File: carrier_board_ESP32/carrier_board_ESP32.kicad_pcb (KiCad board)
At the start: 2 copper layers, 93.5 x 71 mm, 0 parts

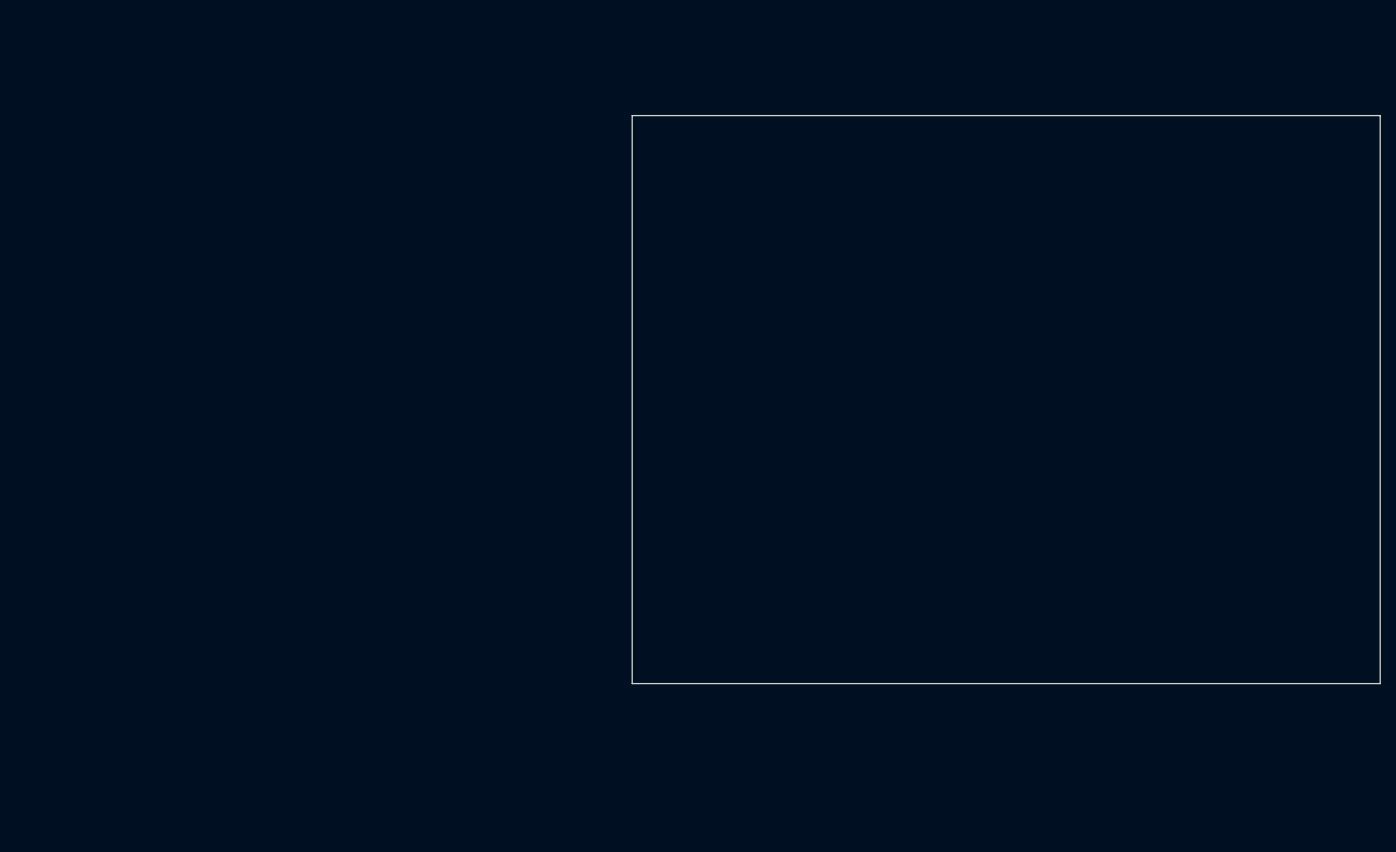
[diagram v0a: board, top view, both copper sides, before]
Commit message: added power supply (battery and solar panel)
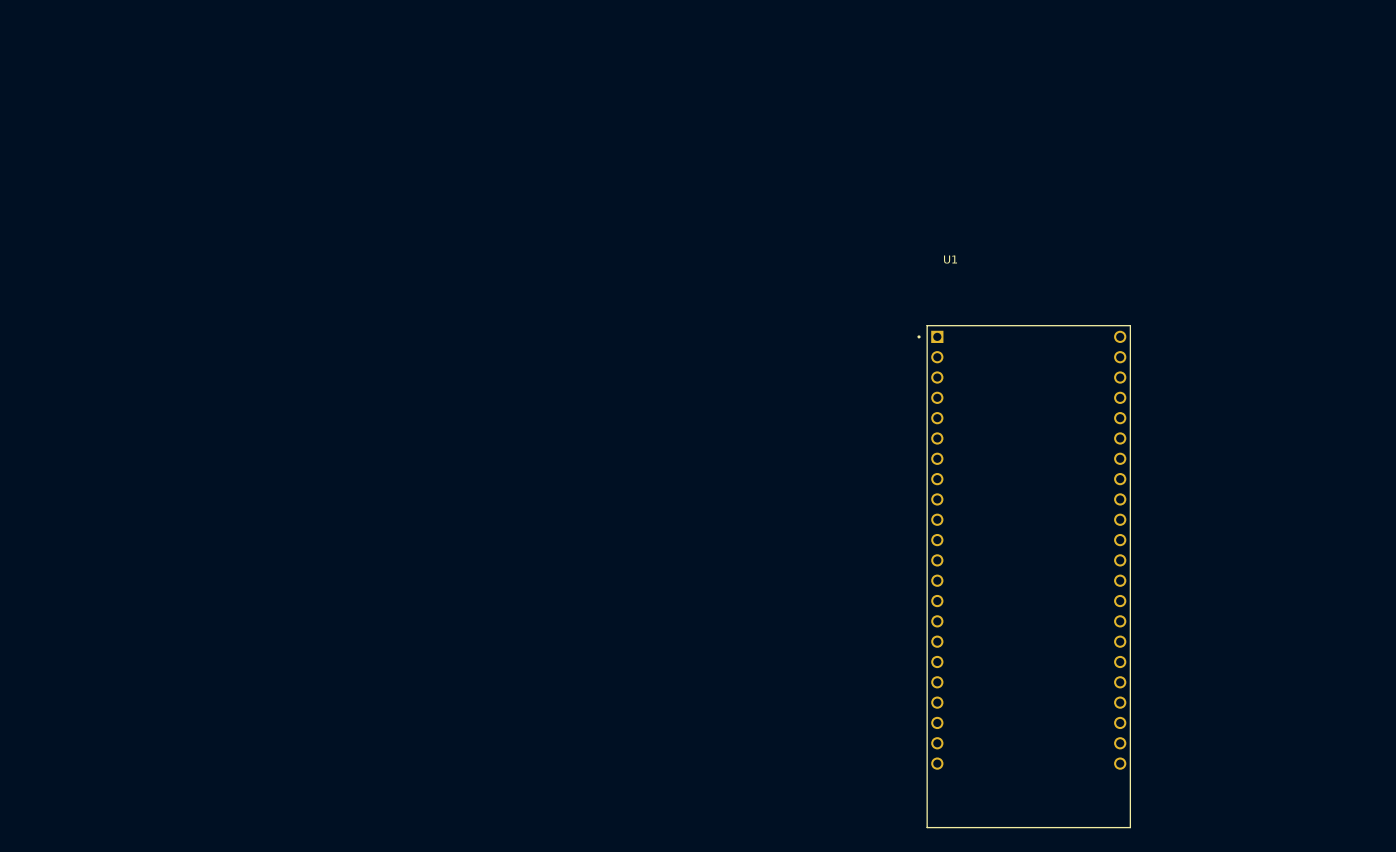
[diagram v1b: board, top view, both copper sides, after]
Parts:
- added U1: ESP32-S3-DEVKITC-1-N8R2, ESP32-S3-DEVKITC-1-N8R2:XCVR_ESP32-S3-DEVKITC-1-N8R2, F.Cu at (147.6, 86.1)
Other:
- board outline removed

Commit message: completed supply section
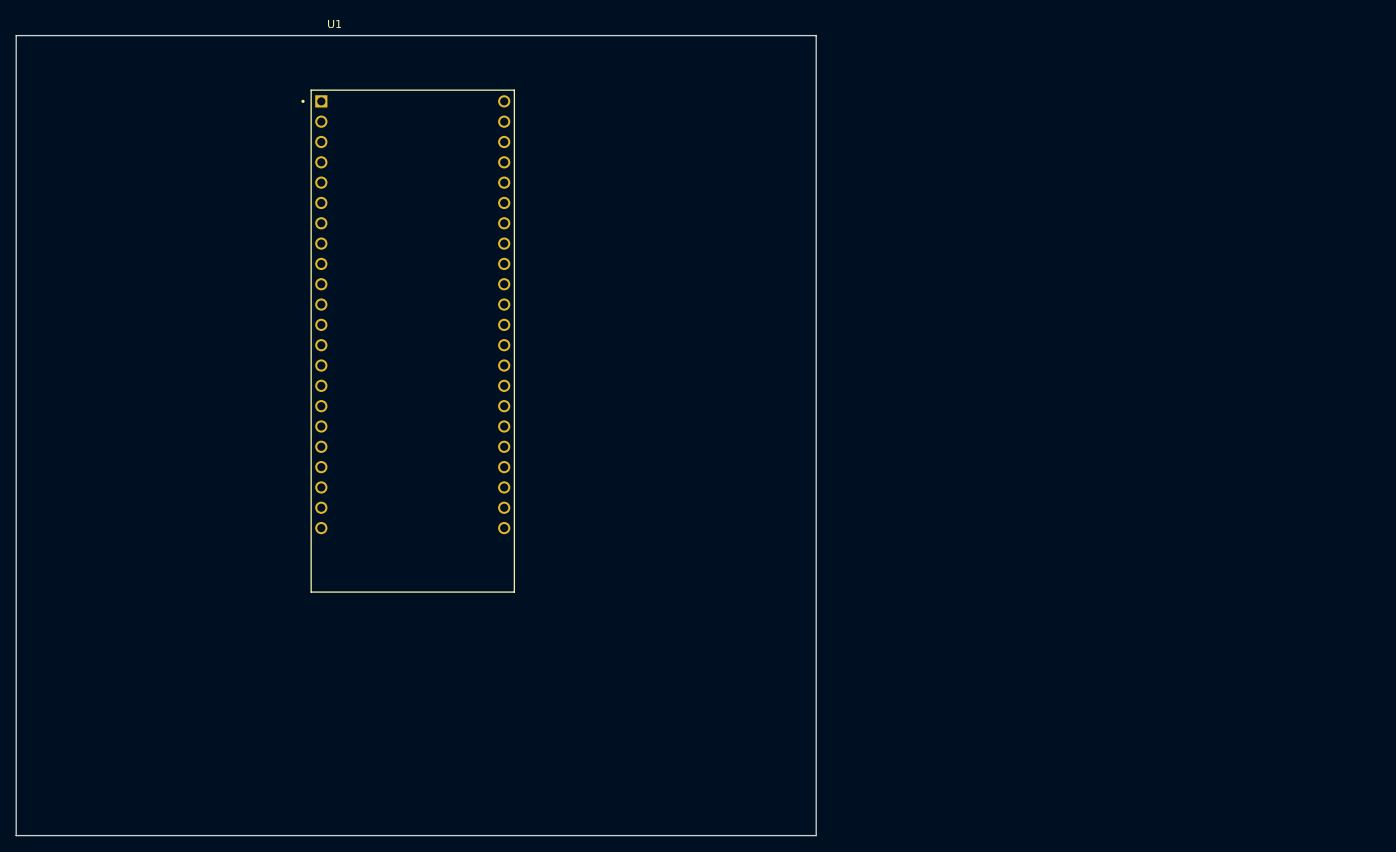
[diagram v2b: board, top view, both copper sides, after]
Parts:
- moved U1 82.4 mm to (70.6, 56.7)
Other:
- board outline added: 100 x 100 mm
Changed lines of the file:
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@@
 	(footprint "ESP32-S3-DEVKITC-1-N8R2:XCVR_ESP32-S3-DEVKITC-1-N8R2"
 		(layer "F.Cu")
-		(at 147.57 86.13)
+		(at 70.57 56.69)
 		(property "Reference" "U1"
 			(at -9.775 -39.605 0)
@@
 		)
 	)
+	(gr_rect
+		(start 21 18.5)
+		(end 121 118.5)
+		(stroke
+			(width 0.05)
+			(type default)
+		)
+		(fill none)
+		(layer "Edge.Cuts")
+	)
 )
